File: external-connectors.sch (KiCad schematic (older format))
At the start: 7 parts

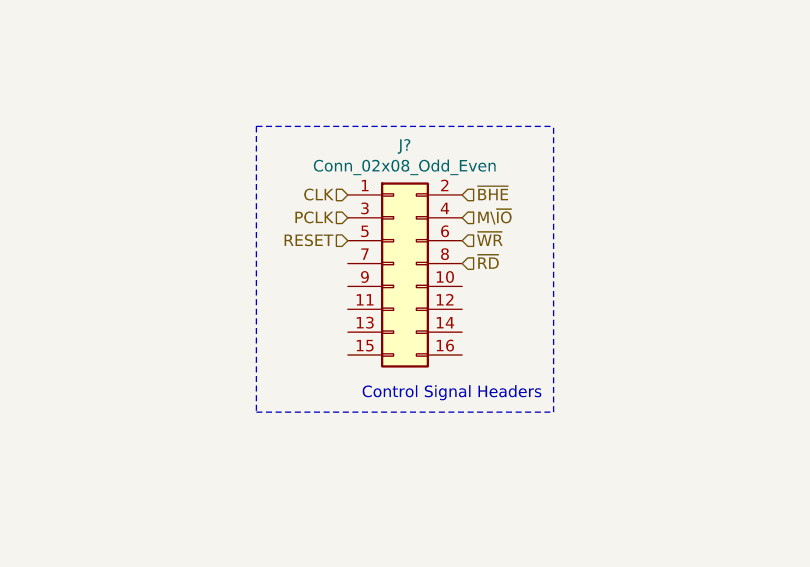
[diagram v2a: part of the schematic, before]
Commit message: General edits; removed floating inputs
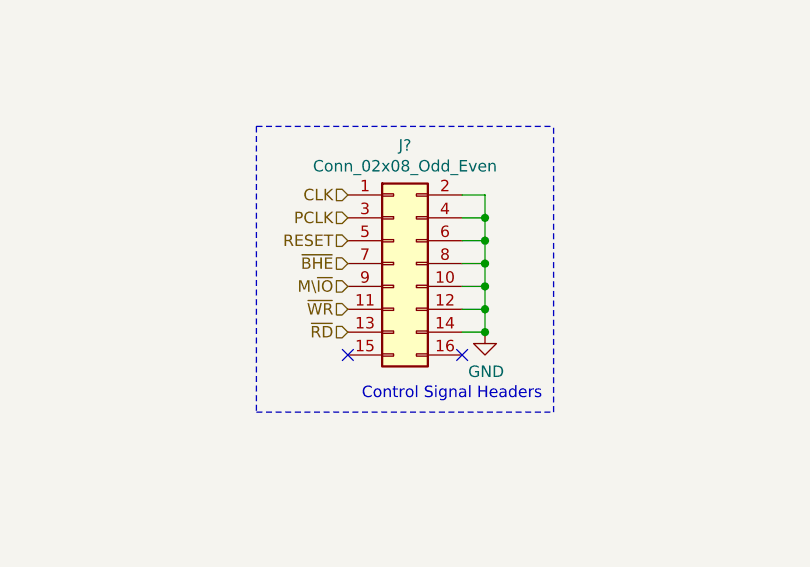
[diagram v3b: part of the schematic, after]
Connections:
- net GND: now also J?.10 (Pin_10), J?.12 (Pin_12), J?.14 (Pin_14), J?.2 (Pin_2), J?.4 (Pin_4), J?.6 (Pin_6), J?.8 (Pin_8)
- net M\~IO: now also J?.9 (Pin_9); no longer J?.4 (Pin_4)
- net ~BHE: now also J?.7 (Pin_7); no longer J?.2 (Pin_2)
- net ~RD: now also J?.13 (Pin_13); no longer J?.8 (Pin_8)
- net ~WR: now also J?.11 (Pin_11); no longer J?.6 (Pin_6)
- no-connect marks 0 -> 2
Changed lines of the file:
@@
 Text HLabel 4100 4950 0    50   Input ~ 0
 RESET
-Text HLabel 4600 4750 2    50   Input ~ 0
+Text HLabel 4100 5050 0    50   Input ~ 0
 ~BHE
 $Comp
@@
 Text Notes 4950 5650 2    50   ~ 0
 Control Signal Headers
+Text HLabel 4100 5150 0    50   Input ~ 0
+M\~IO
+Text HLabel 4100 5250 0    50   Input ~ 0
+~WR
+Text HLabel 4100 5350 0    50   Input ~ 0
+~RD
+NoConn ~ 4100 5450
+NoConn ~ 4600 5450
+Wire Wire Line
+	4600 4750 4700 4750
+Wire Wire Line
+	4700 4750 4700 4850
+Wire Wire Line
+	4700 4850 4600 4850
+Wire Wire Line
+	4600 4950 4700 4950
+Wire Wire Line
+	4700 4950 4700 4850
+Connection ~ 4700 4850
+Wire Wire Line
+	4600 5050 4700 5050
+Wire Wire Line
+	4700 5050 4700 4950
+Connection ~ 4700 4950
+Wire Wire Line
+	4600 5150 4700 5150
+Wire Wire Line
+	4700 5150 4700 5050
+Connection ~ 4700 5050
+Wire Wire Line
+	4600 5250 4700 5250
+Wire Wire Line
+	4700 5250 4700 5150
+Connection ~ 4700 5150
+$Comp
+L power:GND #PWR?
+U 1 1 62100CCC
+P 4700 5350
+F 0 "#PWR?" H 4700 5100 50  0001 C CNN
+F 1 "GND" H 4705 5177 50  0000 C CNN
+F 2 "" H 4700 5350 50  0001 C CNN
+F 3 "" H 4700 5350 50  0001 C CNN
+	1    4700 5350
+	1    0    0    -1
+$EndComp
+Wire Wire Line
+	4600 5350 4700 5350
+Wire Wire Line
+	4700 5250 4700 5350
 Wire Bus Line
 	6050 1950 8100 1950
 Wire Bus Line
 	1900 1950 4650 1950
-Text HLabel 4600 4850 2    50   Input ~ 0
-M\~IO
-Text HLabel 4600 4950 2    50   Input ~ 0
-~WR
-Text HLabel 4600 5050 2    50   Input ~ 0
-~RD
+Connection ~ 4700 5250
+Connection ~ 4700 5350
 $EndSCHEMATC

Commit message: Updates to pass ERC
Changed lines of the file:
@@
 D2
 Text HLabel 6050 1950 0    50   BiDi ~ 0
-DATA_BUS
+D[0..15]
 Text HLabel 4650 1950 2    50   Input ~ 0
-ADDRESS_BUS
+A[0..19]
 Text Label 7000 2050 3    50   ~ 0
 D0
@@
 $EndComp
 Wire Notes Line
-	2250 4800 2250 6700
+	2700 4800 2700 6700
 Wire Notes Line
 	950  4800 950  6700
@@
 	1    0    0    -1
 $EndComp
-Wire Notes Line
-	950  6700 2250 6700
-Wire Notes Line
-	950  4800 2250 4800
 Wire Notes Line
 	3700 4450 3700 5700
@@
 Wire Wire Line
 	4700 5250 4700 5350
+Connection ~ 4700 5250
+Connection ~ 4700 5350
+$Comp
+L power:PWR_FLAG #FLG?
+U 1 1 624921AD
+P 2450 5200
+F 0 "#FLG?" H 2450 5275 50  0001 C CNN
+F 1 "PWR_FLAG" H 2450 5373 50  0000 C CNN
+F 2 "" H 2450 5200 50  0001 C CNN
+F 3 "~" H 2450 5200 50  0001 C CNN
+	1    2450 5200
+	1    0    0    -1
+$EndComp
+$Comp
+L power:PWR_FLAG #FLG?
+U 1 1 62492DD0
+P 2450 6150
+F 0 "#FLG?" H 2450 6225 50  0001 C CNN
+F 1 "PWR_FLAG" H 2450 6323 50  0000 C CNN
+F 2 "" H 2450 6150 50  0001 C CNN
+F 3 "~" H 2450 6150 50  0001 C CNN
+	1    2450 6150
+	1    0    0    -1
+$EndComp
+Wire Wire Line
+	2450 6150 2100 6150
+Connection ~ 2100 6150
+Wire Wire Line
+	2100 5200 2450 5200
+Connection ~ 2100 5200
+Wire Notes Line
+	950  4800 2700 4800
+Wire Notes Line
+	950  6700 2700 6700
+$Comp
+L power:PWR_FLAG #FLG?
+U 1 1 6260FA53
+P 2450 5500
+F 0 "#FLG?" H 2450 5575 50  0001 C CNN
+F 1 "PWR_FLAG" H 2450 5673 50  0000 C CNN
+F 2 "" H 2450 5500 50  0001 C CNN
+F 3 "~" H 2450 5500 50  0001 C CNN
+	1    2450 5500
+	-1   0    0    1
+$EndComp
+Wire Wire Line
+	2450 5500 1850 5500
 Wire Bus Line
 	6050 1950 8100 1950
 Wire Bus Line
 	1900 1950 4650 1950
-Connection ~ 4700 5250
-Connection ~ 4700 5350
+Connection ~ 1850 5500
 $EndSCHEMATC

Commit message: Assign footprints for most symbols
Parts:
- C1, C2: renamed from C?; footprint (none) -> Capacitor_THT:C_Radial_D6.3mm_H5.0mm_P2.50mm
- J3: renamed from J?; footprint (none) -> Connector_PinHeader_2.54mm:PinHeader_2x10_P2.54mm_Vertical
- J4, J5: renamed from J?; footprint (none) -> Connector_PinHeader_2.54mm:PinHeader_2x08_P2.54mm_Vertical
- gave numbers to parts that had none: 2
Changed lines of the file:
@@
 P 3100 2950
 AR Path="/6190420C/62716C16" Ref="J?"  Part="1"
-AR Path="/626E3AF4/62716C16" Ref="J?"  Part="1"
-F 0 "J?" H 3150 3567 50  0000 C CNN
+AR Path="/626E3AF4/62716C16" Ref="J3"  Part="1"
+F 0 "J3" H 3150 3567 50  0000 C CNN
 F 1 "Conn_02x10_Odd_Even" H 3150 3476 50  0000 C CNN
-F 2 "" H 3100 2950 50  0001 C CNN
+F 2 "Connector_PinHeader_2.54mm:PinHeader_2x10_P2.54mm_Vertical" H 3100 2950 50  0001 C CNN
 F 3 "~" H 3100 2950 50  0001 C CNN
 	1    3100 2950
@@
 P 7200 3200
 AR Path="/6190420C/6270A001" Ref="J?"  Part="1"
-AR Path="/626E3AF4/6270A001" Ref="J?"  Part="1"
-F 0 "J?" H 7250 3717 50  0000 C CNN
+AR Path="/626E3AF4/6270A001" Ref="J5"  Part="1"
+F 0 "J5" H 7250 3717 50  0000 C CNN
 F 1 "Conn_02x08_Odd_Even" H 7250 3626 50  0000 C CNN
-F 2 "" H 7200 3200 50  0001 C CNN
+F 2 "Connector_PinHeader_2.54mm:PinHeader_2x08_P2.54mm_Vertical" H 7200 3200 50  0001 C CNN
 F 3 "~" H 7200 3200 50  0001 C CNN
 	1    7200 3200
@@
 P 4300 5050
 AR Path="/6190420C/628395B4" Ref="J?"  Part="1"
-AR Path="/626E3AF4/628395B4" Ref="J?"  Part="1"
-F 0 "J?" H 4350 5567 50  0000 C CNN
+AR Path="/626E3AF4/628395B4" Ref="J4"  Part="1"
+F 0 "J4" H 4350 5567 50  0000 C CNN
 F 1 "Conn_02x08_Odd_Even" H 4350 5476 50  0000 C CNN
-F 2 "" H 4300 5050 50  0001 C CNN
+F 2 "Connector_PinHeader_2.54mm:PinHeader_2x08_P2.54mm_Vertical" H 4300 5050 50  0001 C CNN
 F 3 "~" H 4300 5050 50  0001 C CNN
 	1    4300 5050
@@
 ~BHE
 $Comp
-L power:GND #PWR?
+L power:GND #PWR0101
 U 1 1 61D25BC8
 P 1700 5500
-F 0 "#PWR?" H 1700 5250 50  0001 C CNN
+F 0 "#PWR0101" H 1700 5250 50  0001 C CNN
 F 1 "GND" H 1705 5327 50  0000 C CNN
 F 2 "" H 1700 5500 50  0001 C CNN
@@
 $EndComp
 $Comp
-L power:VCC #PWR?
+L power:VCC #PWR0102
 U 1 1 61D25BCE
 P 2100 5200
-F 0 "#PWR?" H 2100 5050 50  0001 C CNN
+F 0 "#PWR0102" H 2100 5050 50  0001 C CNN
 F 1 "VCC" H 2115 5373 50  0000 C CNN
 F 2 "" H 2100 5200 50  0001 C CNN
@@
 $EndComp
 $Comp
-L Device:C C?
+L Device:C C1
 U 1 1 61D25BD4
 P 1850 5350
-F 0 "C?" H 1965 5396 50  0000 L CNN
+F 0 "C1" H 1965 5396 50  0000 L CNN
 F 1 "100uF" H 1965 5305 50  0000 L CNN
-F 2 "" H 1888 5200 50  0001 C CNN
+F 2 "Capacitor_THT:C_Radial_D6.3mm_H5.0mm_P2.50mm" H 1888 5200 50  0001 C CNN
 F 3 "~" H 1850 5350 50  0001 C CNN
 	1    1850 5350
@@
 P 1250 6250
 AR Path="/61D2B6EC" Ref="J?"  Part="1"
-AR Path="/626E3AF4/61D2B6EC" Ref="J?"  Part="1"
-F 0 "J?" H 1307 6575 50  0000 C CNN
+AR Path="/626E3AF4/61D2B6EC" Ref="J2"  Part="1"
+F 0 "J2" H 1307 6575 50  0000 C CNN
 F 1 "Barrel_Jack +12V" H 1307 6484 50  0000 C CNN
 F 2 "" H 1300 6210 50  0001 C CNN
@@
 $EndComp
 $Comp
-L power:GND #PWR?
+L power:GND #PWR0103
 U 1 1 61D2B6F2
 P 1700 6450
-F 0 "#PWR?" H 1700 6200 50  0001 C CNN
+F 0 "#PWR0103" H 1700 6200 50  0001 C CNN
 F 1 "GND" H 1705 6277 50  0000 C CNN
 F 2 "" H 1700 6450 50  0001 C CNN
@@
 $EndComp
 $Comp
-L Device:C C?
+L Device:C C2
 U 1 1 61D2B6FE
 P 1850 6300
-F 0 "C?" H 1965 6346 50  0000 L CNN
+F 0 "C2" H 1965 6346 50  0000 L CNN
 F 1 "100uF" H 1965 6255 50  0000 L CNN
-F 2 "" H 1888 6150 50  0001 C CNN
+F 2 "Capacitor_THT:C_Radial_D6.3mm_H5.0mm_P2.50mm" H 1888 6150 50  0001 C CNN
 F 3 "~" H 1850 6300 50  0001 C CNN
 	1    1850 6300
@@
 Connection ~ 1700 6450
 $Comp
-L power:+12V #PWR?
+L power:+12V #PWR0104
 U 1 1 61D30CC5
 P 2100 6150
-F 0 "#PWR?" H 2100 6000 50  0001 C CNN
+F 0 "#PWR0104" H 2100 6000 50  0001 C CNN
 F 1 "+12V" H 2115 6323 50  0000 C CNN
 F 2 "" H 2100 6150 50  0001 C CNN
@@
 P 1250 5300
 AR Path="/61D25BC2" Ref="J?"  Part="1"
-AR Path="/626E3AF4/61D25BC2" Ref="J?"  Part="1"
-F 0 "J?" H 1307 5625 50  0000 C CNN
+AR Path="/626E3AF4/61D25BC2" Ref="J1"  Part="1"
+F 0 "J1" H 1307 5625 50  0000 C CNN
 F 1 "Barrel_Jack +5V" H 1307 5534 50  0000 C CNN
 F 2 "" H 1300 5260 50  0001 C CNN
@@
 Connection ~ 4700 5150
 $Comp
-L power:GND #PWR?
+L power:GND #PWR0105
 U 1 1 62100CCC
 P 4700 5350
-F 0 "#PWR?" H 4700 5100 50  0001 C CNN
+F 0 "#PWR0105" H 4700 5100 50  0001 C CNN
 F 1 "GND" H 4705 5177 50  0000 C CNN
 F 2 "" H 4700 5350 50  0001 C CNN
@@
 Connection ~ 4700 5350
 $Comp
-L power:PWR_FLAG #FLG?
+L power:PWR_FLAG #FLG0101
 U 1 1 624921AD
 P 2450 5200
-F 0 "#FLG?" H 2450 5275 50  0001 C CNN
+F 0 "#FLG0101" H 2450 5275 50  0001 C CNN
 F 1 "PWR_FLAG" H 2450 5373 50  0000 C CNN
 F 2 "" H 2450 5200 50  0001 C CNN
@@
 $EndComp
 $Comp
-L power:PWR_FLAG #FLG?
+L power:PWR_FLAG #FLG0102
 U 1 1 62492DD0
 P 2450 6150
-F 0 "#FLG?" H 2450 6225 50  0001 C CNN
+F 0 "#FLG0102" H 2450 6225 50  0001 C CNN
 F 1 "PWR_FLAG" H 2450 6323 50  0000 C CNN
 F 2 "" H 2450 6150 50  0001 C CNN
@@
 	950  6700 2700 6700
 $Comp
-L power:PWR_FLAG #FLG?
+L power:PWR_FLAG #FLG0103
 U 1 1 6260FA53
 P 2450 5500
-F 0 "#FLG?" H 2450 5575 50  0001 C CNN
+F 0 "#FLG0103" H 2450 5575 50  0001 C CNN
 F 1 "PWR_FLAG" H 2450 5673 50  0000 C CNN
 F 2 "" H 2450 5500 50  0001 C CNN
@@
 Wire Wire Line
 	2450 5500 1850 5500
+Connection ~ 1850 5500
 Wire Bus Line
 	6050 1950 8100 1950
 Wire Bus Line
 	1900 1950 4650 1950
-Connection ~ 1850 5500
 $EndSCHEMATC

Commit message: Assigned footprints
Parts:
- C1, C2: symbol Device:C -> Device:CP1
- J1, J2: footprint (none) -> Connector_BarrelJack:BarrelJack_Horizontal
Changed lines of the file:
@@
 $EndComp
 $Comp
-L Device:C C1
+L Device:CP1 C1
 U 1 1 61D25BD4
 P 1850 5350
@@
 F 0 "J2" H 1307 6575 50  0000 C CNN
 F 1 "Barrel_Jack +12V" H 1307 6484 50  0000 C CNN
-F 2 "" H 1300 6210 50  0001 C CNN
+F 2 "Connector_BarrelJack:BarrelJack_Horizontal" H 1300 6210 50  0001 C CNN
 F 3 "~" H 1300 6210 50  0001 C CNN
 	1    1250 6250
@@
 $EndComp
 $Comp
-L Device:C C2
+L Device:CP1 C2
 U 1 1 61D2B6FE
 P 1850 6300
@@
 F 0 "J1" H 1307 5625 50  0000 C CNN
 F 1 "Barrel_Jack +5V" H 1307 5534 50  0000 C CNN
-F 2 "" H 1300 5260 50  0001 C CNN
+F 2 "Connector_BarrelJack:BarrelJack_Horizontal" H 1300 5260 50  0001 C CNN
 F 3 "~" H 1300 5260 50  0001 C CNN
 	1    1250 5300

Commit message: assign footprints and edits
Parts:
- added D12: LED, LED_THT:LED_D5.0mm, symbol Device:LED
- added R23: 330, Resistor_THT:R_Axial_DIN0207_L6.3mm_D2.5mm_P10.16mm_Horizontal, symbol Device:R
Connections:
- net GND: now also D12.1 (K)
- net VCC: now also J4.15 (Pin_15), J4.16 (Pin_16), R23.2
- new net: D12.2 (A), R23.1
- no-connect marks 2 -> 0
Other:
- note added: "PWR LED"
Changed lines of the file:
@@
 $EndComp
 Wire Notes Line
-	3700 4450 3700 5700
-Wire Notes Line
-	3700 5700 5000 5700
-Wire Notes Line
-	5000 5700 5000 4450
+	3700 6000 5000 6000
 Wire Notes Line
 	3700 4450 5000 4450
-Text Notes 4950 5650 2    50   ~ 0
+Text Notes 4950 5950 2    50   ~ 0
 Control Signal Headers
 Text HLabel 4100 5150 0    50   Input ~ 0
@@
 Text HLabel 4100 5350 0    50   Input ~ 0
 ~RD
-NoConn ~ 4100 5450
-NoConn ~ 4600 5450
 Wire Wire Line
 	4600 4750 4700 4750
@@
 L power:GND #PWR0105
 U 1 1 62100CCC
-P 4700 5350
-F 0 "#PWR0105" H 4700 5100 50  0001 C CNN
-F 1 "GND" H 4705 5177 50  0000 C CNN
-F 2 "" H 4700 5350 50  0001 C CNN
-F 3 "" H 4700 5350 50  0001 C CNN
-	1    4700 5350
+P 4700 5600
+F 0 "#PWR0105" H 4700 5350 50  0001 C CNN
+F 1 "GND" H 4705 5427 50  0000 C CNN
+F 2 "" H 4700 5600 50  0001 C CNN
+F 3 "" H 4700 5600 50  0001 C CNN
+	1    4700 5600
 	1    0    0    -1
 $EndComp
@@
 	4700 5250 4700 5350
 Connection ~ 4700 5250
-Connection ~ 4700 5350
 $Comp
 L power:PWR_FLAG #FLG0101
@@
 	2450 5500 1850 5500
 Connection ~ 1850 5500
+Text Notes 7050 4350 0    50   ~ 0
+PWR LED
+$Comp
+L power:VCC #PWR02
+U 1 1 61BA534A
+P 7350 4600
+F 0 "#PWR02" H 7350 4450 50  0001 C CNN
+F 1 "VCC" H 7365 4773 50  0000 C CNN
+F 2 "" H 7350 4600 50  0001 C CNN
+F 3 "" H 7350 4600 50  0001 C CNN
+	1    7350 4600
+	1    0    0    -1
+$EndComp
+$Comp
+L power:GND #PWR03
+U 1 1 61BA5A77
+P 7350 5200
+F 0 "#PWR03" H 7350 4950 50  0001 C CNN
+F 1 "GND" H 7355 5027 50  0000 C CNN
+F 2 "" H 7350 5200 50  0001 C CNN
+F 3 "" H 7350 5200 50  0001 C CNN
+	1    7350 5200
+	1    0    0    -1
+$EndComp
+Wire Wire Line
+	4100 5450 4100 5550
+Wire Wire Line
+	4100 5550 4850 5550
+Wire Wire Line
+	4850 5550 4850 5450
+Wire Wire Line
+	4700 5600 4700 5350
+Connection ~ 4700 5350
+$Comp
+L power:VCC #PWR01
+U 1 1 61BBFA03
+P 4850 4850
+F 0 "#PWR01" H 4850 4700 50  0001 C CNN
+F 1 "VCC" H 4865 5023 50  0000 C CNN
+F 2 "" H 4850 4850 50  0001 C CNN
+F 3 "" H 4850 4850 50  0001 C CNN
+	1    4850 4850
+	1    0    0    -1
+$EndComp
+Wire Wire Line
+	4600 5450 4850 5450
+Connection ~ 4850 5450
+Wire Wire Line
+	4850 5450 4850 4850
+Wire Notes Line
+	5000 4450 5000 6000
+Wire Notes Line
+	3700 4450 3700 6000
+$Comp
+L Device:LED D?
+U 1 1 61BD0CAA
+P 7350 5050
+AR Path="/61CCC9EF/61BD0CAA" Ref="D?"  Part="1"
+AR Path="/626E3AF4/61BD0CAA" Ref="D12"  Part="1"
+F 0 "D12" H 7343 5267 50  0000 C CNN
+F 1 "LED" H 7343 5176 50  0000 C CNN
+F 2 "LED_THT:LED_D5.0mm" H 7350 5050 50  0001 C CNN
+F 3 "~" H 7350 5050 50  0001 C CNN
+	1    7350 5050
+	0    -1   -1   0
+$EndComp
+$Comp
+L Device:R R23
+U 1 1 61BD3D88
+P 7350 4750
+F 0 "R23" H 7281 4704 50  0000 R CNN
+F 1 "330" H 7281 4795 50  0000 R CNN
+F 2 "Resistor_THT:R_Axial_DIN0207_L6.3mm_D2.5mm_P10.16mm_Horizontal" V 7280 4750 50  0001 C CNN
+F 3 "~" H 7350 4750 50  0001 C CNN
+	1    7350 4750
+	1    0    0    1
+$EndComp
+Wire Notes Line
+	7050 4250 7050 5450
+Wire Notes Line
+	7050 5450 7550 5450
+Wire Notes Line
+	7550 5450 7550 4250
+Wire Notes Line
+	7050 4250 7550 4250
 Wire Bus Line
 	6050 1950 8100 1950

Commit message: begin pcb layout
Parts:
- D12: value LED -> PWR LED
- J3: value Conn_02x10_Odd_Even -> ADDRESS BUS
- J4: value Conn_02x08_Odd_Even -> CONTROL BUS
- J5: value Conn_02x08_Odd_Even -> DATA BUS
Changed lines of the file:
@@
 AR Path="/626E3AF4/62716C16" Ref="J3"  Part="1"
 F 0 "J3" H 3150 3567 50  0000 C CNN
-F 1 "Conn_02x10_Odd_Even" H 3150 3476 50  0000 C CNN
+F 1 "ADDRESS BUS" H 3150 3476 50  0000 C CNN
 F 2 "Connector_PinHeader_2.54mm:PinHeader_2x10_P2.54mm_Vertical" H 3100 2950 50  0001 C CNN
 F 3 "~" H 3100 2950 50  0001 C CNN
@@
 AR Path="/626E3AF4/6270A001" Ref="J5"  Part="1"
 F 0 "J5" H 7250 3717 50  0000 C CNN
-F 1 "Conn_02x08_Odd_Even" H 7250 3626 50  0000 C CNN
+F 1 "DATA BUS" H 7250 3626 50  0000 C CNN
 F 2 "Connector_PinHeader_2.54mm:PinHeader_2x08_P2.54mm_Vertical" H 7200 3200 50  0001 C CNN
 F 3 "~" H 7200 3200 50  0001 C CNN
@@
 AR Path="/626E3AF4/628395B4" Ref="J4"  Part="1"
 F 0 "J4" H 4350 5567 50  0000 C CNN
-F 1 "Conn_02x08_Odd_Even" H 4350 5476 50  0000 C CNN
+F 1 "CONTROL BUS" H 4350 5476 50  0000 C CNN
 F 2 "Connector_PinHeader_2.54mm:PinHeader_2x08_P2.54mm_Vertical" H 4300 5050 50  0001 C CNN
 F 3 "~" H 4300 5050 50  0001 C CNN
@@
 AR Path="/626E3AF4/61BD0CAA" Ref="D12"  Part="1"
 F 0 "D12" H 7343 5267 50  0000 C CNN
-F 1 "LED" H 7343 5176 50  0000 C CNN
+F 1 "PWR LED" H 7343 5176 50  0000 C CNN
 F 2 "LED_THT:LED_D5.0mm" H 7350 5050 50  0001 C CNN
 F 3 "~" H 7350 5050 50  0001 C CNN
